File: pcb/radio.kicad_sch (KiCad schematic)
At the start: 0 parts

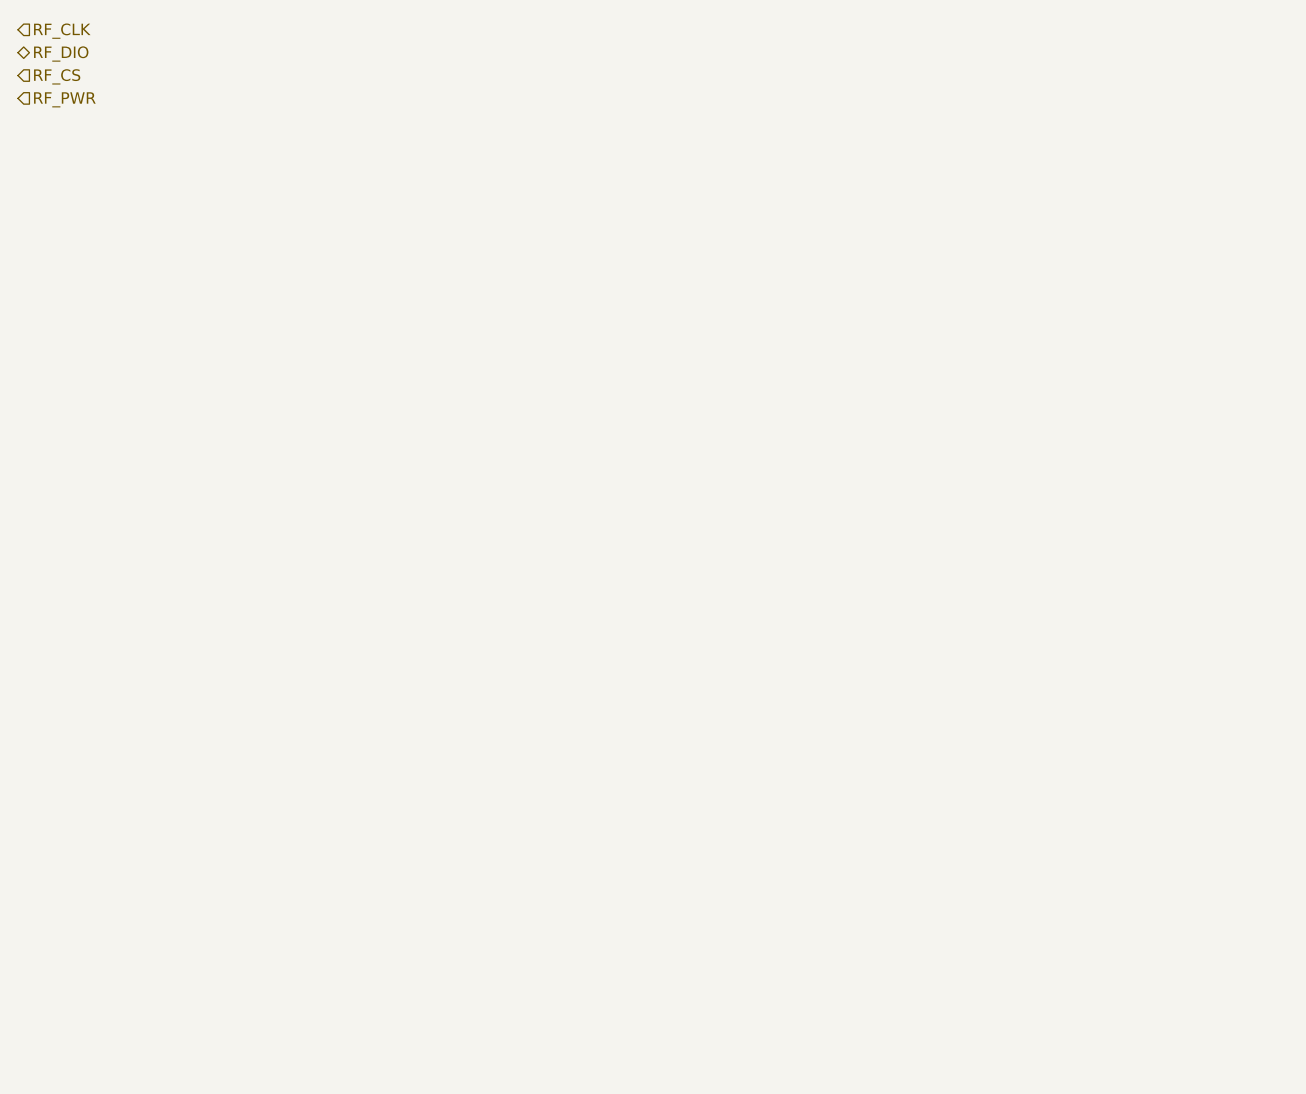
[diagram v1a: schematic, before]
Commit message: draw the radio sheet, and its symbol
The last empty sheet is populated, so the rules check is down to the two long-known items: the
flash symbol's hand-placed fields, and the hub's open-collector fault outputs, which the check
counts as undriven inputs because the pull-up is inside the hub. Sixteen of the twenty-one
violations were the empty sheet's own interface, and they are gone.

The module is Raspberry Pi's Radio Module 2. Two pre-certified modules carry this silicon and only
one brings out the serial host interface the proven firmware speaks -- the other offers the wider
bus only, which the driver cannot use -- so the choice was made by the driver rather than by any
electrical comparison. No stock symbol exists for it, so it is drawn into the project library that
was standing empty for exactly this.

Drawing it added parts the four-signal interface did not imply. One host pin serves three of the
module's pads: data in takes the line directly, data out reaches it through 470 ohms so that a
collision damages neither end and whichever is driving wins, and the interrupt reaches it through
10k, large enough to pull the shared line without disturbing traffic on it. Both values are the
module vendor's. The two radios enable on separate pads, tied together here because nothing wants
one without the other. All six ground pads go to the plane rather than the convenient few, because
the module asks for a good ground for the sake of its antenna.

Three things were recorded rather than solved. The bus timing is specified against a 125 MHz system
clock and ours is nearly double, so the divisor has to be re-derived -- firmware, but a consequence
of the clock decision and better recorded against it than found at bring-up. The antenna keep-out
is now a stated constraint rather than a guess: metal-free off the antenna end, good ground
elsewhere, and no ground poured near the antenna. And the module's -30C to +70C range is narrower
than anything else here, so it bounds the produ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
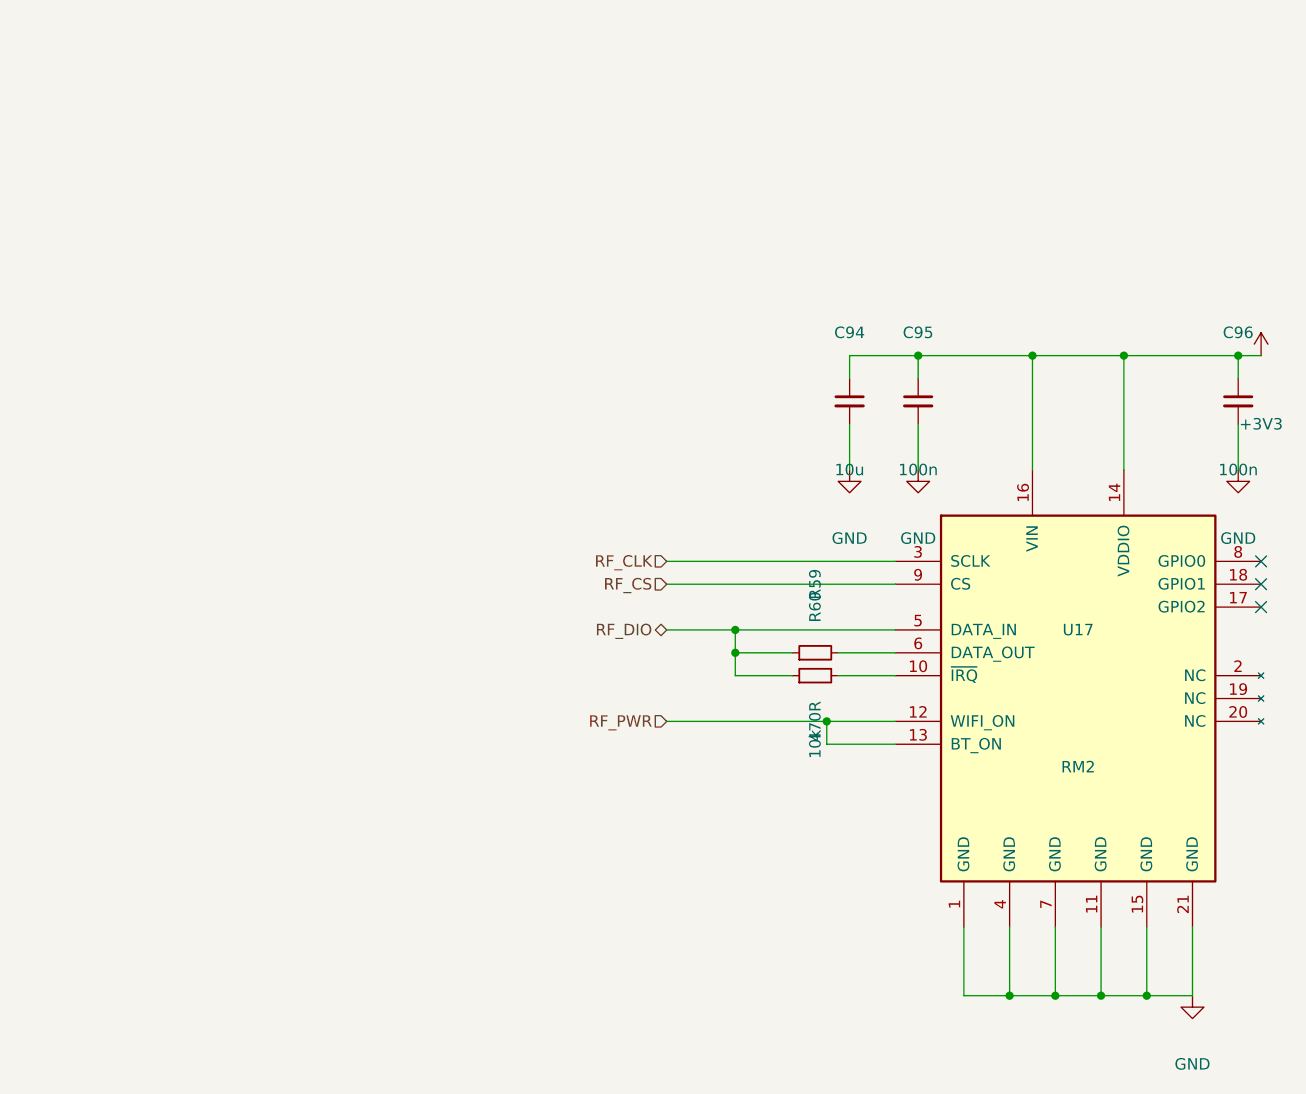
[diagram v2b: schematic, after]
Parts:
- added C94: 10u, symbol Device:C_Small
- added C95, C96: 100n, symbol Device:C_Small
- added R59: 470R, symbol Device:R_Small
- added R60: 10k, symbol Device:R_Small
- added U17: RM2, symbol crossfire:RM2
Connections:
- net RF_CLK: now also U17.3 (SCLK)
- net RF_CS: now also U17.9 (CS)
- net RF_DIO: now also R59.1, R60.1, U17.5 (DATA_IN)
- net RF_PWR: now also U17.12 (WIFI_ON), U17.13 (BT_ON)
- new net: R59.2, U17.6 (DATA_OUT)
- new net: R60.2, U17.10 (~{IRQ})
- new net +3V3: C94.1, C95.1, C96.1, U17.14 (VDDIO), U17.16 (VIN)
- new net GND: C94.2, C95.2, C96.2, U17.1 (GND), U17.11 (GND), U17.15 (GND), U17.21 (GND), U17.4 (GND), U17.7 (GND)
- no-connect marks 0 -> 3

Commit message: specify every capacitor: a rating and a dielectric, chosen from its net
A value on its own is not a specification. Each of the 62 capacitor symbols now carries a voltage
rating and a dielectric picked from the net it sits on -- at least twice the working voltage,
rounded to a standard rating, and never below what a socket the user can reach can present. Both
are hidden fields, so the drawing stays readable and a bill of materials can still be made from it.

Two of the choices are decisions rather than arithmetic.

The connector-side parts are rated for abuse at 50V, because nothing on the board protects them:
both input switches sit downstream of them, so the sink's own supply decoupling and the data
port's see whatever a hostile charger produces with no switch in between.

The charger's input bank is rated 25V on a condition, and the condition is firmware. The input
over-voltage trip defaults to 26V, which is above a 25V part, so rating the bank for its working
voltage is only safe if that trip comes down. The part offers 7V, 12V, 22V and 26V and 12V is the
right one here: the sink never asks for more than 9V, so 12V clears the profile with room and
bounds what the bank can ever see. A board decision that creates a firmware requirement is exactly
the sort that gets lost, so it is recorded on both sides.

What is left open is what the banks are worth once fitted. The charger specifies them as counts of
10uF parts, which only means something if each part is still worth 10uF where it sits, and a
ceramic at 9V is not. The rating and the dielectric are settled; the package is not, and the
package is what decides how much survives. The footprint step has to read each chosen part's bias
curve and add parts if the effective value falls short rather than assume the count was the point.
That is the one piece of this specification that can still change the part count.

Rules check unchanged, and the schematic check is clean.

Co-Authored-By: Claude Opus 5 (1M context) <norepl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
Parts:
- C94, C95, C96: Dielectric (none) -> X7R; Voltage (none) -> 16V
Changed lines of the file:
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@@
+			)
+		)
+		(property "Voltage" "16V"
+			(at 152.40 88.90 0)
+			(show_name no)
+			(do_not_autoplace no)
+			(effects
+				(font
+					(size 1.27 1.27)
+				)
+				(hide yes)
+			)
+		)
+		(property "Dielectric" "X7R"
+			(at 152.40 88.90 0)
+			(show_name no)
+			(do_not_autoplace no)
+			(effects
+				(font
+					(size 1.27 1.27)
+				)
+				(hide yes)
 			)
 		)
@@
 			)
 		)
+		(property "Voltage" "16V"
+			(at 160.02 88.90 0)
+			(show_name no)
+			(do_not_autoplace no)
+			(effects
+				(font
+					(size 1.27 1.27)
+				)
+				(hide yes)
+			)
+		)
+		(property "Dielectric" "X7R"
+			(at 160.02 88.90 0)
+			(show_name no)
+			(do_not_autoplace no)
+			(effects
+				(font
+					(size 1.27 1.27)
+				)
+				(hide yes)
+			)
+		)
 		(pin "1"
 		)		(pin "2"
@@
 			)
 		)
+		(property "Voltage" "16V"
+			(at 195.58 88.90 0)
+			(show_name no)
+			(do_not_autoplace no)
+			(effects
+				(font
+					(size 1.27 1.27)
+				)
+				(hide yes)
+			)
+		)
+		(property "Dielectric" "X7R"
+			(at 195.58 88.90 0)
+			(show_name no)
+			(do_not_autoplace no)
+			(effects
+				(font
+					(size 1.27 1.27)
+				)
+				(hide yes)
+			)
+		)

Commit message: specify the resistors, and round three values that were never parts
Every resistor now carries a tolerance, and it is 1% only where the value is read: a reference a
part trims itself against, a divider ratio, a termination that states what this end of a cable is,
a value that programs a threshold at power-on. Nineteen of the thirty-eight qualify; the rest are
pull-ups, pull-downs, straps and series parts, where 5% is honest and 1% buys nothing. Power is not
a field, because the largest dissipation anywhere on the board is a few milliwatts in an
indicator's series resistor.

Three values were arithmetic nobody had rounded. 5.24k and 30.31k are the charger vendor's own
calculated figures for the temperature network and neither exists as a part; 172k was ours for the
boost's current limit and is not a standard value either. They become 5.23k, 30.1k and 174k, and
what each costs is recorded: a fraction of a degree on the temperature thresholds, about 2% on the
current limit. A fourth, the hub's reference resistor, had its tolerance written into the value
string; that moves to the field where it belongs.

Reading the boost's datasheet to round the current limit corrected how it had been described. The
limit is not set at the worst-case peak -- the switch has to pass about 4.25A at the bottom of the
cell with every port loaded, so a limit there would trip in normal service. It sits at about 5.9A,
clearing that peak by nearly 40%. The vendor publishes two resistances against measured limits,
which fixes both the relationship and its direction: more resistance, less current.

Rules check unchanged, schematic check clean.

Co-Authored-By: Claude Opus 5 (1M context) <noreply@anthropic.com>
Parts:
- R59, R60: Tolerance (none) -> 5%
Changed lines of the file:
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@@
+			)
+		)
+		(property "Tolerance" "5%"
+			(at 148.59 116.84 0)
+			(show_name no)
+			(do_not_autoplace no)
+			(effects
+				(font
+					(size 1.27 1.27)
+				)
+				(hide yes)
 			)
 		)
@@
 			)
 		)
+		(property "Tolerance" "5%"
+			(at 148.59 119.38 0)
+			(show_name no)
+			(do_not_autoplace no)
+			(effects
+				(font
+					(size 1.27 1.27)
+				)
+				(hide yes)
+			)
+		)

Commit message: calculate the capacitor banks, and give every one of them a package
The question a value and a rating leave open is how much capacitance is actually there once the
voltage is across it, and the answer differs by package for the same value and rating. So the
requirement is derived bank by bank rather than taken from the vendors' part counts.

The charger's input is the binding case. Holding its input ripple to 100 mV with 5.4 A through the
inductor needs 8.6uF in circuit out of the 20uF fitted, so 43% has to survive 9V. The 5V rail needs
36% of what it carries and the system rail 27%. That last one is worth stating properly: ripple
alone would want only 2.5uF there, so the bank exists to answer load steps, and the realistic fast
step is the radio transmitting and the processor waking rather than the ports, which cannot step
quickly because the boost soft-starts over 4ms. At half an amp over five microseconds that is 25uF
against about 70uF effective.

43% is comfortable in 1206 and marginal in 0603 for a 10uF part at 9V, so the five capacitors on
the 9V nodes take 1206 and everything at 4.5V or under takes 0805. Decoupling goes to 0402, where
being near the pin matters more than the package, and the frequency- and loop-setting parts to
0603, where there is nothing to derate.

The answer to the open item is that the counts do not change: every bank is adequate as drawn
provided each part keeps roughly half of itself, which is what the package choice delivers. What is
left is a purchasing check rather than a design one.

Two asymmetries recorded. The 3.3V converter's vendor states that its recommended values anticipate
tolerance and bias derating and quotes 20% and 50%, so its table is nominal with the margin already
in it; the charger's and the boost's say nothing, so there the derating is ours to carry. And the
processor specifies an effective tolerance rather than a nominal one -- its core regulator's output
capacitor must be 4.7uF +/-20% in circuit.

The checker's 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
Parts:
- C94: footprint (none) -> Capacitor_SMD:C_0805_2012Metric
- C95, C96: footprint (none) -> Capacitor_SMD:C_0402_1005Metric
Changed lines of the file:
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@@
+			)
+		)
+		(property "Footprint" "Capacitor_SMD:C_0805_2012Metric"
+			(at 152.40 88.90 0)
+			(show_name no)
+			(do_not_autoplace no)
+			(effects
+				(font
+					(size 1.27 1.27)
+				)
+				(hide yes)
 			)
 		)
@@
 			)
 		)
+		(property "Footprint" "Capacitor_SMD:C_0402_1005Metric"
+			(at 160.02 88.90 0)
+			(show_name no)
+			(do_not_autoplace no)
+			(effects
+				(font
+					(size 1.27 1.27)
+				)
+				(hide yes)
+			)
+		)
 		(property "Voltage" "16V"
 			(at 160.02 88.90 0)
@@
 			)
 		)
+		(property "Footprint" "Capacitor_SMD:C_0402_1005Metric"
+			(at 195.58 88.90 0)
+			(show_name no)
+			(do_not_autoplace no)
+			(effects
+				(font
+					(size 1.27 1.27)
+				)
+				(hide yes)
+			)
+		)

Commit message: assign the footprints, and take the radio module's from its vendor
132 of the 135 parts now carry a footprint. Most follow from the package, the capacitors' follow
from the bias calculation, and the resistors are 0603 rather than 0402 because the board has room,
the first one runs bare on a bench, and a part you can get a probe or an iron onto is worth more
there than the millimetre it saves.

The radio module nearly went in hand-drawn. It has no footprint in any stock library, so the
obvious move was to draw one from the dimension drawing in its datasheet; the pitch, pad size and
pad length read off cleanly, but where each pad sits along its edge did not, and what I had was
inference from where things appeared in a rendered figure rather than a stated number. Raspberry Pi
publish a KiCad symbol and footprint, so that is what is fitted, in a project footprint library
beside the project symbol library. The figure agreed on everything it stated plainly, which says
nothing about the parts it did not.

Taking the official symbol also checked this project's hand-drawn one against theirs. All 21 pins
agree. Four carry different names -- their DI and DO, their nIRQ and WL_ON -- and nothing else
differs, so the pin numbering derived from the module's table is confirmed against its author
rather than merely self-consistent.

Four packages are fitted provisionally and are recorded as such, because what is unsettled about
them is invisible: the processor, the hub, the 3.3V converter and the power sink are in packages
whose library entries differ only in the size of the pad under the part. Body, pitch and pin count
are right; the pad is the nearest variant and wants checking against each vendor's land pattern,
since too small costs thermal performance and too large can wick the part off its pins.

Three parts are deliberately left without one. For the remaining inductors the footprint is the
part -- pad geometry differs between vendors at the same nominal size -- so choosing an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
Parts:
- R59, R60: footprint (none) -> Resistor_SMD:R_0603_1608Metric
- U17: footprint (none) -> crossfire:rpi_rmc20452t
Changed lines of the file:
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@@
+			)
+		)
+		(property "Footprint" "crossfire:rpi_rmc20452t"
+			(at 177.80 121.92 0)
+			(show_name no)
+			(do_not_autoplace no)
+			(effects
+				(font
+					(size 1.27 1.27)
+				)
+				(hide yes)
 			)
 		)
@@
 			)
 		)
+		(property "Footprint" "Resistor_SMD:R_0603_1608Metric"
+			(at 148.59 116.84 0)
+			(show_name no)
+			(do_not_autoplace no)
+			(effects
+				(font
+					(size 1.27 1.27)
+				)
+				(hide yes)
+			)
+		)
 		(property "Tolerance" "5%"
 			(at 148.59 116.84 0)
@@
 			)
 		)
+		(property "Footprint" "Resistor_SMD:R_0603_1608Metric"
+			(at 148.59 119.38 0)
+			(show_name no)
+			(do_not_autoplace no)
+			(effects
+				(font
+					(size 1.27 1.27)
+				)
+				(hide yes)
+			)
+		)
